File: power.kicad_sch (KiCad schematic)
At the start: 34 parts, among them Q4 Q_PMOS_GDS, Q5 BC856, U11 MAX17634BATP+, U12 AP62250WU

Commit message: WIP: display
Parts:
- C30, C31: Voltage (none) -> 50V
- renumbered U11 to U12, U12 to U13
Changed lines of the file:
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@@
   )
   (symbol (lib_id "Device:C") (at 101.6 93.98 0) (unit 1)
-    (in_bom yes) (on_board yes) (fields_autoplaced)
+    (in_bom yes) (on_board yes)
     (property "Reference" "C31" (id 0) (at 105.41 92.7099 0)
       (effects (font (size 1.27 1.27)) (justify left))
@@
     (property "Datasheet" "~" (id 3) (at 101.6 93.98 0)
       (effects (font (size 1.27 1.27)) hide)
+    )
+    (property "Voltage" "50V" (id 4) (at 105.41 97.79 0)
+      (effects (font (size 1 1)) (justify left))
     )
     (pin "1")
@@
   (symbol (lib_id "AP6230xWU:AP6230xWU") (at 139.7 152.4 0) (unit 1)
     (in_bom yes) (on_board yes)
-    (property "Reference" "U12" (id 0) (at 139.7 143.51 0))
+    (property "Reference" "U13" (id 0) (at 139.7 143.51 0))
     (property "Value" "AP62250WU" (id 1) (at 139.7 146.05 0))
     (property "Footprint" "TSOT26:TSOT26" (id 2) (at 139.7 152.4 0)
@@
   )
   (symbol (lib_id "Device:C") (at 88.9 93.98 0) (unit 1)
-    (in_bom yes) (on_board yes) (fields_autoplaced)
+    (in_bom yes) (on_board yes)
     (property "Reference" "C30" (id 0) (at 92.71 92.7099 0)
       (effects (font (size 1.27 1.27)) (justify left))
@@
     (property "Datasheet" "~" (id 3) (at 88.9 93.98 0)
       (effects (font (size 1.27 1.27)) hide)
+    )
+    (property "Voltage" "50V" (id 4) (at 92.71 97.79 0)
+      (effects (font (size 1 1)) (justify left))
     )
     (pin "1")
@@
   (symbol (lib_id "MAX17634BATP_:MAX17634BATP+") (at 139.7 101.6 0) (unit 1)
     (in_bom yes) (on_board yes) (fields_autoplaced)
-    (property "Reference" "U11" (id 0) (at 139.7 81.28 0))
+    (property "Reference" "U12" (id 0) (at 139.7 81.28 0))
     (property "Value" "MAX17634BATP+" (id 1) (at 139.7 83.82 0))
     (property "Footprint" "MAX17634:TQFN20-EP" (id 2) (at 139.7 101.6 0)

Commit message: Should be final
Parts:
- C33, C34, C39, C40: footprint Capacitor_SMD:C_1206_3216Metric -> Capacitor_SMD:C_0805_2012Metric
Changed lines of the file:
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@@
       (effects (font (size 1.27 1.27)) (justify left))
     )
-    (property "Footprint" "Capacitor_SMD:C_1206_3216Metric" (id 2) (at 216.8652 105.41 0)
+    (property "Footprint" "Capacitor_SMD:C_0805_2012Metric" (id 2) (at 216.8652 105.41 0)
       (effects (font (size 1.27 1.27)) hide)
     )
@@
       (effects (font (size 1.27 1.27)) (justify left))
     )
-    (property "Footprint" "Capacitor_SMD:C_1206_3216Metric" (id 2) (at 216.8652 158.75 0)
+    (property "Footprint" "Capacitor_SMD:C_0805_2012Metric" (id 2) (at 216.8652 158.75 0)
       (effects (font (size 1.27 1.27)) hide)
     )
@@
       (effects (font (size 1.27 1.27)) (justify left))
     )
-    (property "Footprint" "Capacitor_SMD:C_1206_3216Metric" (id 2) (at 204.1652 158.75 0)
+    (property "Footprint" "Capacitor_SMD:C_0805_2012Metric" (id 2) (at 204.1652 158.75 0)
       (effects (font (size 1.27 1.27)) hide)
     )
@@
       (effects (font (size 1.27 1.27)) (justify left))
     )
-    (property "Footprint" "Capacitor_SMD:C_1206_3216Metric" (id 2) (at 204.1652 105.41 0)
-      (effects (font (size 1.27 1.27)) hide)
-    )
+    (property "Footprint" "Capacitor_SMD:C_0805_2012Metric" (id 2) (at 204.1652 105.41 0)
+      (effects (font (size 1.27 1.27)) hide)
+    )

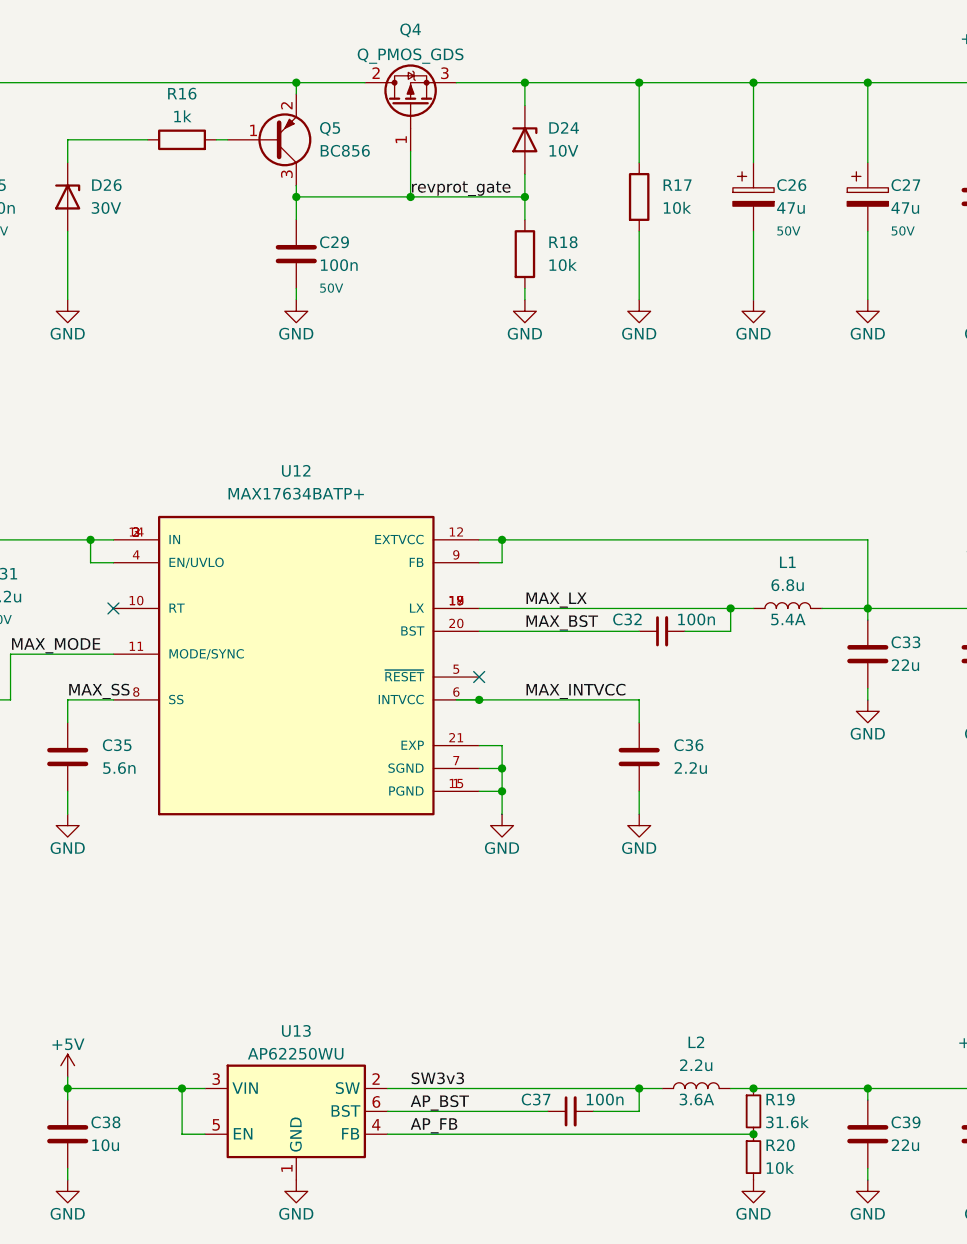
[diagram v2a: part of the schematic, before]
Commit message: rev1.1: Add I2C pullups
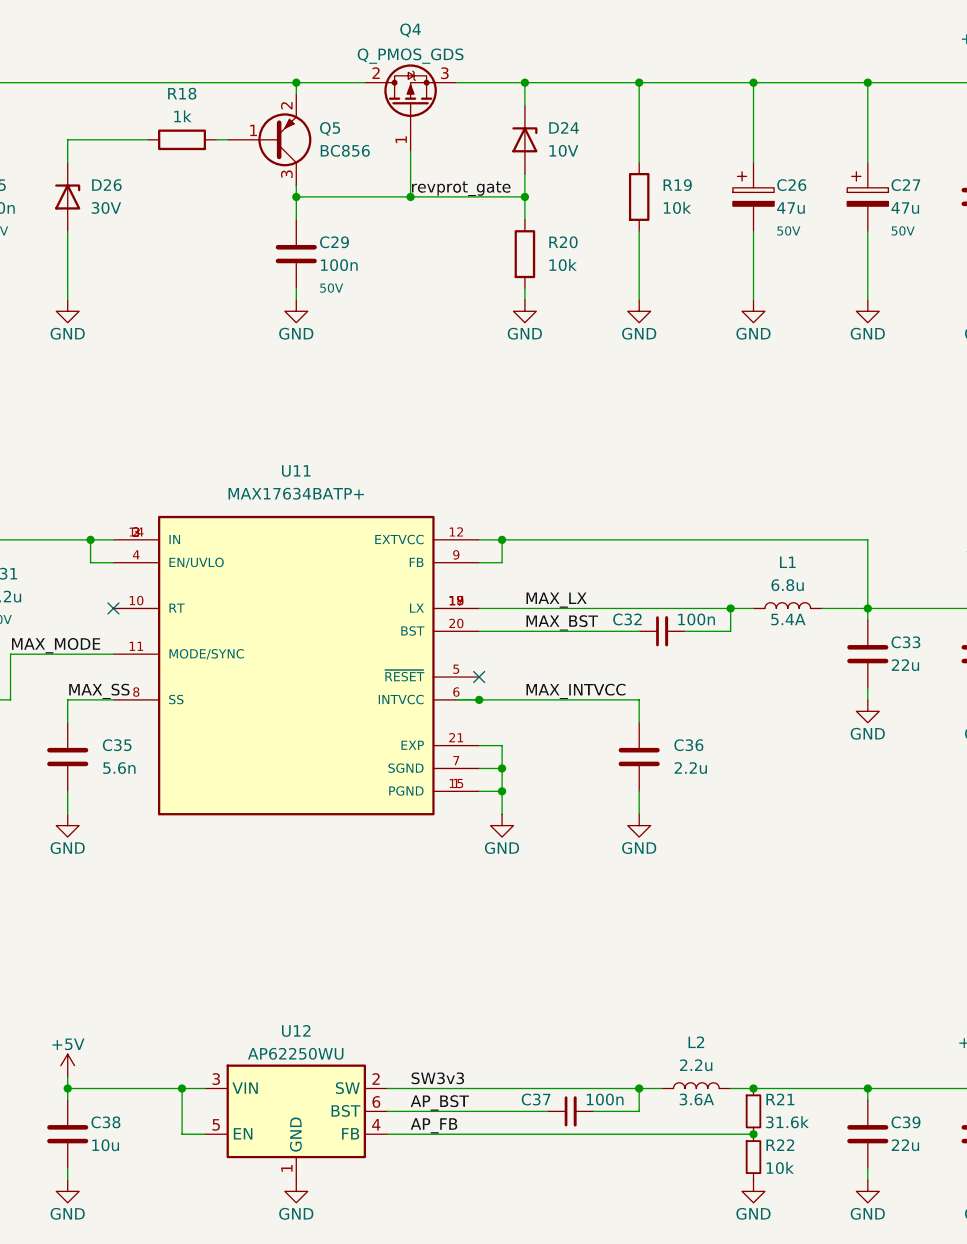
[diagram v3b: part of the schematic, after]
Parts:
- renumbered R16 to R18, R17 to R19, R18 to R20, R19 to R21, R20 to R22, U12 to U11, U13 to U12

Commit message: lots changed
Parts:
- removed Q4: Q_PMOS_GDS, Package_TO_SOT_SMD:TO-252-2, symbol Device:Q_PMOS_GDS
- added Q12: TPCP8110, TPCP8110:PS-8, symbol TPCP8110:TPCP8110
- C26: renamed from C29; Voltage 50V -> 100V
- F8: renamed from F9; footprint Littelfuse-154:Littelfuse-154 -> Littelfuse-154:Littelfuse-154-2920
- renumbered C25 to C22, C26 to C23, C27 to C24, C28 to C25, C30 to C27, C31 to C28, C32 to C29, C33 to C30, C34 to C31, C35 to C32, C36 to C33, C37 to C34, C38 to C35, C39 to C36, C40 to C37, D24 to D20, D25 to D21, D26 to D22, JP38 to JP10, JP39 to JP11, Q5 to Q13, R18 to R36, R19 to R37, R20 to R38, R21 to R39, R22 to R40, U12 to U10, U11 to U9
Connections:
- net +24V: now also Q12.1 (S), Q12.2 (S), Q12.3 (S)
- net Fused24V: now also Q12.5 (D), Q12.6 (D), Q12.7 (D), Q12.8 (D)
- net revprot_gate: now also Q12.4 (G)

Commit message: things changed
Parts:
- added FB1, FB2: 220, Inductor_SMD:L_1206_3216Metric, symbol Device:FerriteBead_Small
- added R51: 56k, Resistor_SMD:R_0603_1608Metric, symbol Device:R
- added R52: 10k, Resistor_SMD:R_0603_1608Metric, symbol Device:R
- U10: renamed from U9; value MAX17634BATP+ -> MAX17633BATP+; A_MAX 0.8 -> (none); B_MAX 0.3 -> (none); B_MIN 0.2 -> (none); B_NOM 0.25 -> (none); D2_NOM 2.9 -> (none); D_MAX 4.1 -> (none); D_MIN 3.9 -> (none); D_NOM 4.0 -> (none); E2_NOM 2.9 -> (none); ENOM 0.5 -> (none); E_MAX 4.1 -> (none); E_MIN 3.9 -> (none); E_NOM 4.0 -> (none); L_MAX 0.35 -> (none); L_MIN 0.25 -> (none); L_NOM 0.3 -> (none); MANUFACTURER Maxim Integrated -> (none); PARTREV Rev 0; 6/19 -> (none); PIN_COUNT_D 5.0 -> (none); PIN_COUNT_E 5.0 -> (none); STANDARD IPC 7351B -> (none)
- renumbered C22 to C34, C23 to C35, C24 to C36, C25 to C37, C26 to C38, C27 to C39, C28 to C40, C29 to C41, C30 to C42, C31 to C43, C32 to C44, C33 to C45, C34 to C46, C35 to C47, C36 to C48, C37 to C49, D20 to D19, D21 to D20, D22 to D21, JP10 to JP6, JP11 to JP7, Q12 to Q20, Q13 to Q21, R36 to R48, R37 to R49, R38 to R50, R39 to R53, R40 to R54, U10 to U11
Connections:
- net +24V: now also R51.1; no longer U10.4 (EN/UVLO)
- net +5V: no longer U11.5 (EN)
- net Fused24V: now also FB1.1; no longer C34.1, D20.2 (A2), Q20.5 (D), Q20.6 (D), Q20.7 (D), Q20.8 (D), Q21.2 (E)
- net GND: now also R52.2
- net MAX_~{RST}: now reaches U10.5 (~{RESET})
- net MAX_~{RST}: now also U11.5 (EN)
- new net: C34.1, FB2.2, Q20.5 (D), Q20.6 (D), Q20.7 (D), Q20.8 (D), Q21.2 (E)
- new net: D20.2 (A2), FB1.2, FB2.1
- new net MAX_EN: R51.2, R52.1, U10.4 (EN/UVLO)
- no-connect marks 2 -> 1
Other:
- note added: "3.5A max"
- note added: "Internal 2.5ms soft start"
- note added: "~1ms soft start"
- moved on the sheet: C41, C44, C45, JP6, JP7

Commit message: isolate and other stuff
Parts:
- C33: renamed from C34; footprint Capacitor_SMD:C_0805_2012Metric -> Capacitor_SMD:C_1206_3216Metric
- C37: renamed from C38; footprint Capacitor_SMD:C_0805_2012Metric -> Capacitor_SMD:C_1206_3216Metric
- FB1, FB2: value 220 -> 100
- renumbered C35 to C34, C36 to C35, C37 to C36, C39 to C38, C40 to C39, C41 to C40, C42 to C41, C43 to C42, C44 to C43, C45 to C44, C46 to C45, C47 to C46, C48 to C47, C49 to C48, D19 to D21, D20 to D22, D21 to D23, F8 to F9, JP6 to JP5, JP7 to JP6, Q20 to Q21, Q21 to Q22, R48 to R53, R49 to R54, R50 to R55, R51 to R56, R52 to R57, R53 to R58, R54 to R59, U11 to U10, U10 to U9
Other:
- title: [canbrd] CAN/RS485 IO board -> [canbrd] CAN IO board

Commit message: things changed
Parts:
- removed Q21: TPCP8110, TPCP8110:PS-8, symbol TPCP8110:TPCP8110
- added Q22, Q23: Q_PMOS_GDS, Package_TO_SOT_SMD:TO-252-2, symbol Device:Q_PMOS_GDS
- added R58: 50m, Resistor_SMD:R_0612_1632Metric, symbol Device:R
- added R60: 10k, Resistor_SMD:R_0603_1608Metric, symbol Device:R
- added R63: 5.1k, Resistor_SMD:R_0603_1608Metric, symbol Device:R
- added R64: 1k, Resistor_SMD:R_0603_1608Metric, symbol Device:R
- added U10: ZXCT1109, Package_TO_SOT_SMD:SOT-23, symbol Amplifier_Current:ZXCT1109
- D30: renamed from D22; value 33V -> 30V; Field4 SMAJ33CA -> SMBJ30CA
- F9: footprint Littelfuse-154:Littelfuse-154-2920 -> keystone-3522:Keystone_3522
- renumbered C33 to C43, C34 to C44, C35 to C45, C36 to C46, C37 to C47, C38 to C48, C39 to C49, C40 to C50, C41 to C51, C42 to C52, C43 to C53, C44 to C54, C45 to C55, C46 to C56, C47 to C57, C48 to C58, D21 to D29, D23 to D31, JP5 to JP7, JP6 to JP8, Q22 to Q24, R53 to R59, R54 to R61, R55 to R62, R56 to R65, R57 to R66, R58 to R67, R59 to R68, U9 to U11, U10 to U12
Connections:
- net +24V: now also R58.2, R60.1, U10.1 (Vs-); no longer C44.1, C45.1, C46.1, D29.1 (K), R61.1
- net GND: now also R63.2, R64.2
- net revprot_gate: now also Q22.1 (G), Q23.1 (G)
- net pmos_drain: now reaches C43.1, FB2.2, Q24.2 (E)
- net pmos_drain: now also Q22.2 (D)
- net +3V3 renamed +3.3V
- new net: D29.1 (K), Q22.3 (S), Q23.3 (S)
- new net 24Vpre: C44.1, C45.1, C46.1, Q23.2 (D), R58.1, R61.1, U10.2 (Vs+)
- new net I_meas: R63.1, U10.3 (OUT)
- new net U_meas: R60.2, R64.1
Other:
- note added: "0.0909 V/V"
- note added: "1.04 V/A"
- moved on the sheet: C44, C45, C46, R61, R62

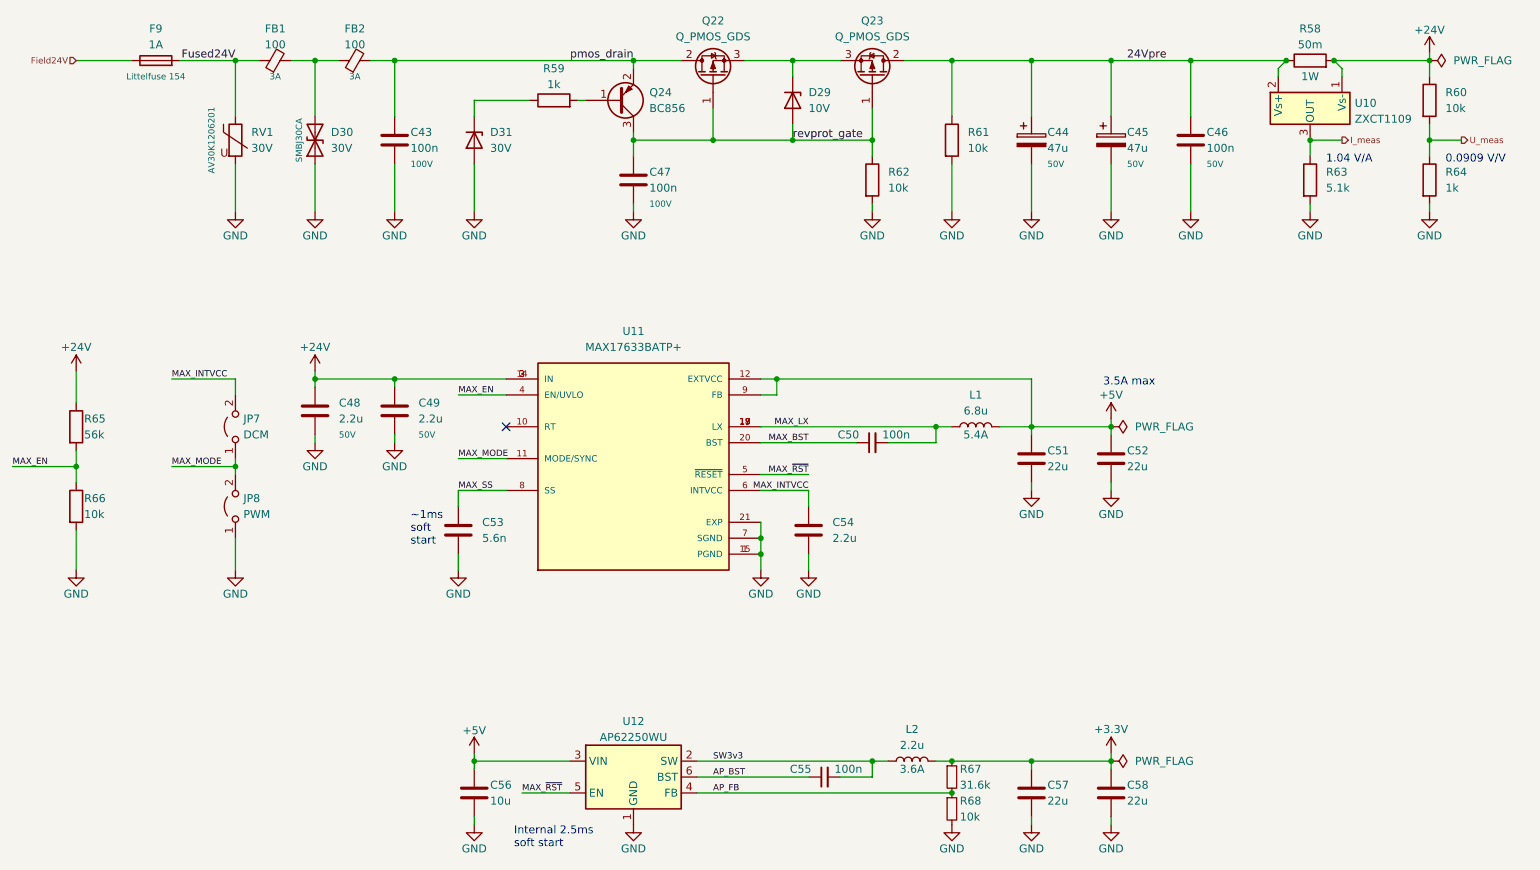
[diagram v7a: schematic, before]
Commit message: Minimal design for testing
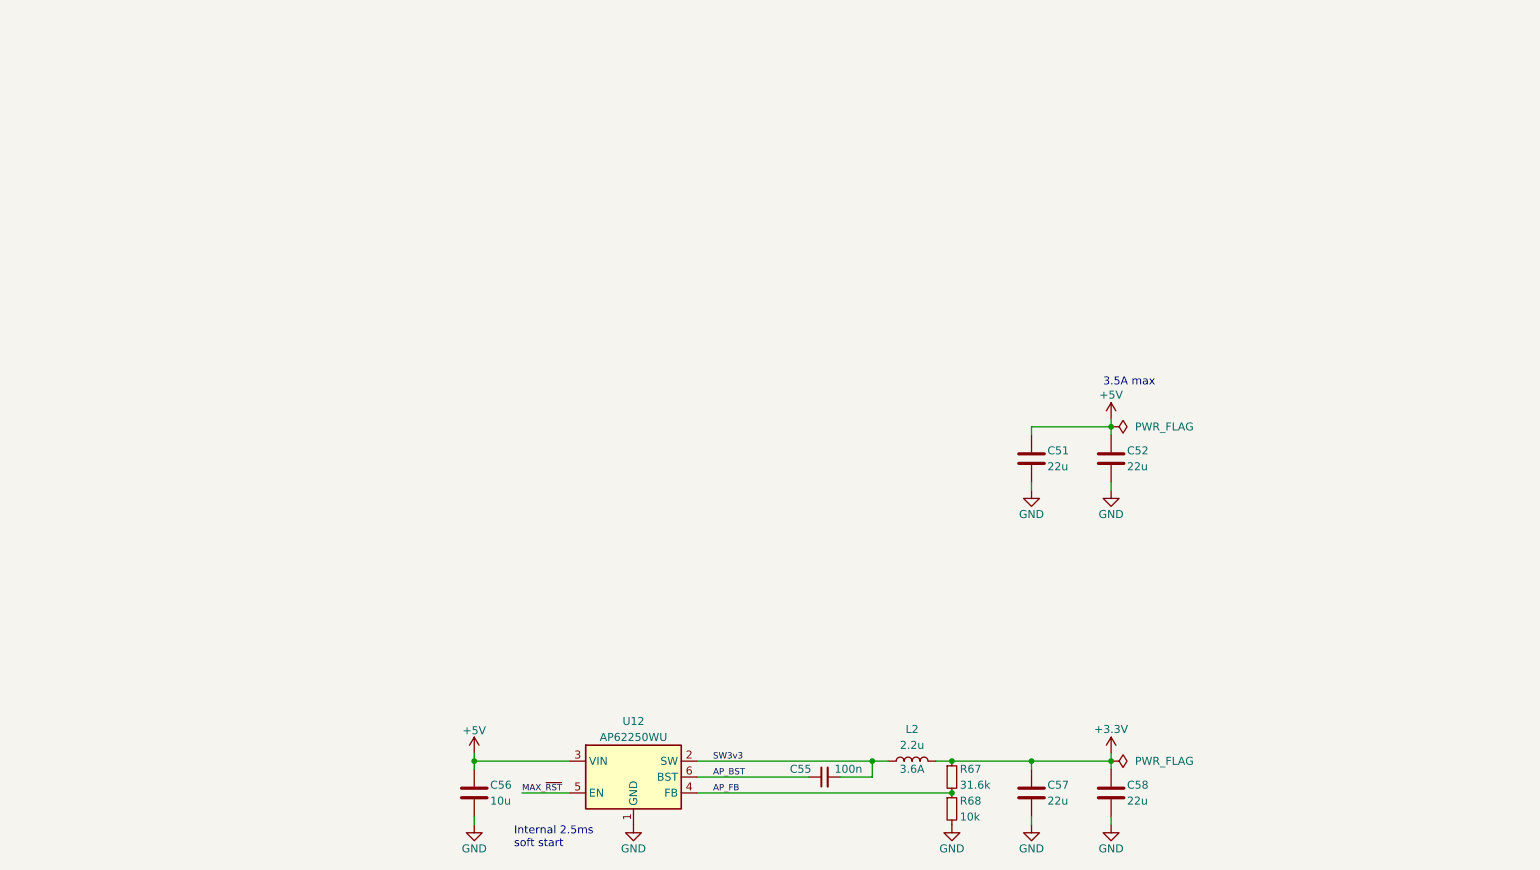
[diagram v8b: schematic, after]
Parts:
- removed C43, C47: 100n, Capacitor_SMD:C_1206_3216Metric, symbol Device:C
- removed C44, C45: 47u, Capacitor_SMD:CP_Elec_8x6.5, symbol Device:C_Polarized
- removed C46: 100n, Capacitor_SMD:C_0805_2012Metric, symbol Device:C
- removed C48, C49: 2.2u, Capacitor_SMD:C_1206_3216Metric, symbol Device:C
- removed C50: 100n, Capacitor_SMD:C_0603_1608Metric, symbol Device:C_Small
- removed C53: 5.6n, Capacitor_SMD:C_0603_1608Metric, symbol Device:C
- removed C54: 2.2u, Capacitor_SMD:C_0603_1608Metric, symbol Device:C
- removed D29: 10V, Diode_SMD:D_SOD-123, symbol Device:D_Zener
- removed D30: 30V, Diode_SMD:D_SMB, symbol Device:D_TVS
- removed D31: 30V, Diode_SMD:D_SOD-123, symbol Device:D_Zener
- removed F9: 1A, keystone-3522:Keystone_3522, symbol Device:Fuse
- removed FB1, FB2: 100, Inductor_SMD:L_1206_3216Metric, symbol Device:FerriteBead_Small
- removed JP7: DCM, Jumper:SolderJumper-2_P1.3mm_Open_TrianglePad1.0x1.5mm, symbol Jumper:Jumper_2_Open
- removed JP8: PWM, Jumper:SolderJumper-2_P1.3mm_Open_TrianglePad1.0x1.5mm, symbol Jumper:Jumper_2_Open
- removed L1: 6.8u, Inductor_SMD:L_Abracon_ASPI-0630LR, symbol Device:L
- removed Q22, Q23: Q_PMOS_GDS, Package_TO_SOT_SMD:TO-252-2, symbol Device:Q_PMOS_GDS
- removed Q24: BC856, Package_TO_SOT_SMD:SOT-23, symbol Transistor_BJT:BC856
- removed R58: 50m, Resistor_SMD:R_0612_1632Metric, symbol Device:R
- removed R59, R64: 1k, Resistor_SMD:R_0603_1608Metric, symbol Device:R
- removed R60, R61, R62, R66: 10k, Resistor_SMD:R_0603_1608Metric, symbol Device:R
- removed R63: 5.1k, Resistor_SMD:R_0603_1608Metric, symbol Device:R
- removed R65: 56k, Resistor_SMD:R_0603_1608Metric, symbol Device:R
- removed RV1: 30V, Resistor_SMD:R_1206_3216Metric, symbol Device:Varistor
- removed U10: ZXCT1109, Package_TO_SOT_SMD:SOT-23, symbol Amplifier_Current:ZXCT1109
- removed U11: MAX17633BATP+, MAX17634:TQFN20-EP, symbol MAX17634BATP_:MAX17634BATP+
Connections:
- no-connect marks 1 -> 0
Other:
- note removed: "0.0909 V/V"
- note removed: "1.04 V/A"
- note removed: "~1ms soft start"
